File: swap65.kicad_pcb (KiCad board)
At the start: 2 copper layers, 309.6 x 100 mm, 168 parts, among them J1 USB_C_Receptacle_USB2.0, J2 OLED, J3 DB, SW1 SW_Push, SW10 A, SW11 Z, SW12 LWin, SW13 2, SW14 W, SW15 S, SW16 X, SW17 LAlt, SW18 3, SW19 E, SW2 SW_Push, SW20 D, SW21 C, SW22 4, SW23 R, SW24 F, SW25 V, SW26 5, SW27 T, SW28 G, SW29 B, SW3 Esc, SW30 Space, SW31 6, SW32 Y, SW33 H, SW34 N, SW35 7, SW36 U, SW37 J, SW38 M, SW39 8, SW4 Tab, SW40 I, SW41 K, SW42 Comma, SW43 9, SW44 O, SW45 L, SW46 Period, SW47 RAlt, SW48 0, SW49 P, SW5 Caps, SW50 Colon, SW51 Slash, SW52 Fn, SW53 Minus, SW54 [, SW55 Quote, SW56 Plus, SW57 ], SW58 RShift, SW59 Left, SW6 LShift, SW60 Pipe, SW61 BkSlsh, SW62 Enter, SW63 Up, SW64 Down, SW65 BkSpc, SW66 Tilde, SW67 Right, SW7 LCtrl, SW8 1, SW9 Q, U1 RP2040, U2 SRV05-4, U3 W25Q128JVS, U4 XC6206PxxxMR, Y1 12MHz

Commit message: routed mcu
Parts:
- moved U3 12.3 mm to (359.8, 124.2)
- moved SW1 12.2 mm to (359.1, 106.8)
- moved C1 11.7 mm to (358.4, 129.7), turned to 0 degrees
- moved R5 10.8 mm to (357.9, 113.6)
- moved R3 8.20 mm to (344.8, 146.7), turned to 0 degrees
- moved SW2 4.39 mm to (347.2, 151.7), turned to 90 degrees
- moved R1 1.33 mm to (356.4, 129.2)
- moved C13 1.31 mm to (348.4, 132.5), turned to 180 degrees
- moved C12 1.13 mm to (353.1, 128.5)
- moved C8 1.13 mm to (354.1, 128.5)
- moved R2 0.97 mm to (355.2, 129.2)
- moved C7 0.93 mm to (347.3, 137.4)
- moved R4 0.89 mm to (350.3, 140.5)
- moved C2 0.89 mm to (348.3, 143.8)
- moved C3 0.89 mm to (348.3, 139.8)
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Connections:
- U1 pad 38: SCL -> SDA
- U1 pad 39: SDA -> SCL
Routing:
- net COL1: track 0.00 -> 105.4 mm
- net COL2: track 0.00 -> 96.4 mm
- net COL13: track 0.00 -> 93.8 mm
- net COL9: track 0.00 -> 92.6 mm
- net COL10: track 0.00 -> 92.3 mm
- net COL3: track 0.00 -> 91.7 mm
- net COL5: track 0.00 -> 90.8 mm
- net COL0: track 0.00 -> 90.8 mm
- net COL12: track 0.00 -> 87.8 mm
- net COL14: track 0.00 -> 79.5 mm
- net COL7: track 0.00 -> 72.7 mm
- net COL8: track 0.00 -> 72.6 mm
- net COL6: track 0.00 -> 71.3 mm
- net +3V3: track 2.80 -> 73.5 mm
- net COL4: track 0.00 -> 70.1 mm
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- added copper zone on B.Cu, net GND

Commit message: second pass at routing complete
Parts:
- moved D10 4.77 mm to (99.2, 181.8)
- moved D5 4.77 mm to (75.4, 181.8)
- moved D15 4.76 mm to (123.0, 181.8)
- moved D45 4.76 mm to (265.9, 181.8)
- moved D50 4.76 mm to (289.7, 181.8)
- moved D49 3.22 mm to (287.3, 162.7)
- moved D14 3.21 mm to (134.9, 162.7)
- moved D19 3.21 mm to (154.0, 162.7)
- moved D27 3.21 mm to (192.1, 162.7)
- moved D36 3.21 mm to (230.2, 162.7)
- moved D4 3.21 mm to (84.9, 162.7)
- moved D40 3.21 mm to (249.2, 162.7)
- moved D44 3.21 mm to (268.3, 162.7)
- moved D56 3.21 mm to (313.5, 162.7)
- moved D61 3.21 mm to (339.7, 162.7)
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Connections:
- U1 pad 11: COL6 -> COL7
- U1 pad 12: COL5 -> COL6
- U1 pad 13: COL4 -> COL5
- U1 pad 14: COL3 -> COL4
- U1 pad 15: COL2 -> COL3
- U1 pad 16: COL1 -> COL2
- U1 pad 17: COL0 -> COL1
- U1 pad 18: unconnected-(U1-Pad18) -> COL0
- U1 pad 2: COL14 -> ROW4
- U1 pad 29: ROW4 -> unconnected-(U1-Pad29)
- U1 pad 3: COL13 -> COL14
- U1 pad 4: COL12 -> COL13
- U1 pad 5: COL11 -> COL12
- U1 pad 6: COL10 -> COL11
- U1 pad 7: COL9 -> COL10
- U1 pad 8: COL8 -> COL9
- U1 pad 9: COL7 -> COL8
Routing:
- net ROW4: track 3.87 -> 333.0 mm
- net COL0: track 90.8 -> 402.5 mm
- net ROW0: track 5.69 -> 297.6 mm
- net ROW3: track 3.53 -> 292.8 mm
- net COL1: track 105.4 -> 393.8 mm
- net ROW1: track 5.61 -> 276.3 mm
- net ROW2: track 4.58 -> 274.8 mm
- net COL2: track 96.4 -> 361.0 mm
- net COL4: track 70.1 -> 297.2 mm, vias 0 -> 1
- net COL3: track 91.7 -> 313.1 mm, vias 0 -> 1
- net COL5: track 90.8 -> 286.4 mm
- net COL6: track 71.3 -> 261.8 mm, vias 0 -> 1
- net COL7: track 72.7 -> 245.3 mm, vias 0 -> 1
- net COL8: track 72.6 -> 224.9 mm, vias 0 -> 1
- net COL9: track 92.6 -> 219.0 mm
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
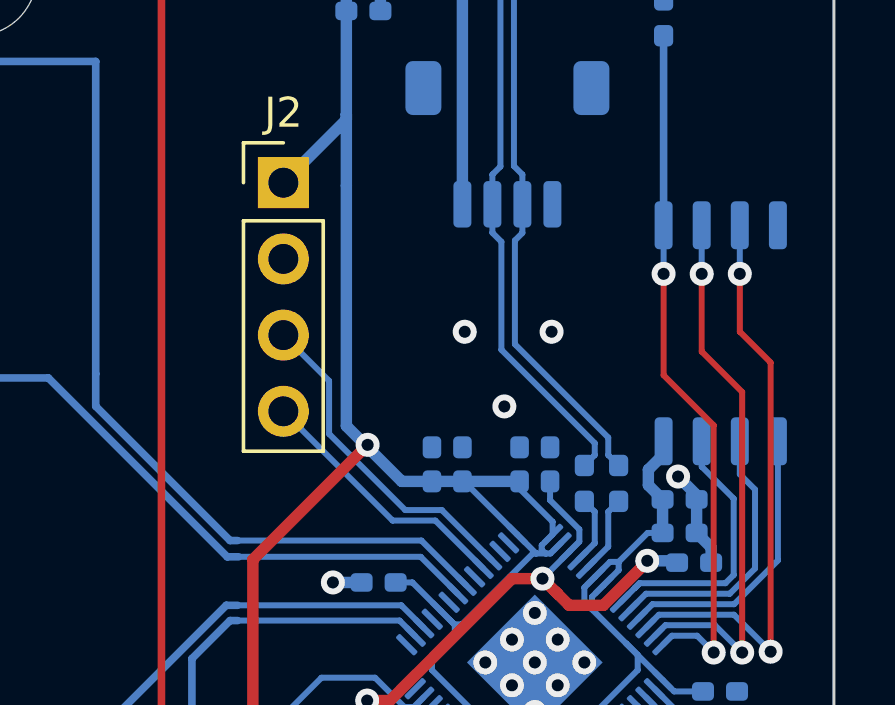
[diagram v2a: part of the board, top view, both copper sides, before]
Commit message: fixed courtyard overlap
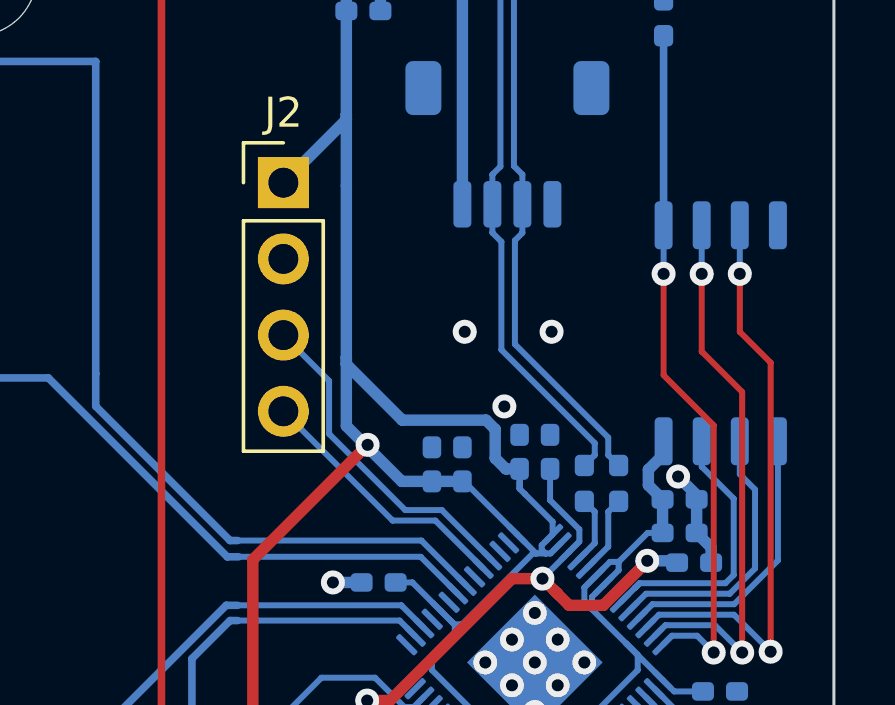
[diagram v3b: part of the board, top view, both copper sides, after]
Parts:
- moved C12 0.42 mm to (353.1, 128.1)
- moved C8 0.42 mm to (354.1, 128.1)
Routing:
- net +3V3: track 94.0 -> 100.8 mm
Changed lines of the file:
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@@
   )
   (footprint "Capacitor_SMD:C_0402_1005Metric_Pad0.74x0.62mm_HandSolder" (layer "B.Cu")
-    (at 353.06 128.524 90)
+    (at 353.06 128.1089 90)
     (descr "Capacitor SMD 0402 (1005 Metric), square (rectangular) end terminal, IPC_7351 nominal with elongated pad for handsoldering. (Body size source: IPC-SM-782 page 76, https://www.pcb-3d.com/wordpress/wp-content/uploads/ipc-sm-782a_amendment_1_and_2.pdf), generated with kicad-footprint-generator")
     (tags "capacitor handsolder")
@@
   )
   (footprint "Capacitor_SMD:C_0402_1005Metric_Pad0.74x0.62mm_HandSolder" (layer "B.Cu")
-    (at 354.076 128.524 90)
+    (at 354.076 128.1089 90)
     (descr "Capacitor SMD 0402 (1005 Metric), square (rectangular) end terminal, IPC_7351 nominal with elongated pad for handsoldering. (Body size source: IPC-SM-782 page 76, https://www.pcb-3d.com/wordpress/wp-content/uploads/ipc-sm-782a_amendment_1_and_2.pdf), generated with kicad-footprint-generator")
     (tags "capacitor handsolder")
@@
   (via (at 347.98 136.398) (size 0.8) (drill 0.4) (layers "F.Cu" "B.Cu") (net 1))
   (via (at 357.316566 131.739166) (size 0.8) (drill 0.4) (layers "F.Cu" "B.Cu") (net 1))
-  (segment (start 355.052404 131.098011) (end 355.052404 130.694204) (width 0.2) (layer "B.Cu") (net 1))
   (segment (start 347.98 136.398) (end 347.98 137.3465) (width 0.381) (layer "B.Cu") (net 1))
+  (segment (start 355.052404 131.098011) (end 355.052404 130.694204) (width 0.2) (layer "B.Cu") (net 1))
   (segment (start 357.239677 131.739166) (end 357.316566 131.739166) (width 0.2) (layer "B.Cu") (net 1))
+  (segment (start 354.725887 131.424528) (end 355.052404 131.098011) (width 0.2) (layer "B.Cu") (net 1))
+  (segment (start 354.076 129.7178) (end 354.076 128.6764) (width 0.2) (layer "B.Cu") (net 1))
   (segment (start 347.959432 137.460932) (end 350.386539 137.460932) (width 0.2) (layer "B.Cu") (net 1))
   (segment (start 347.9125 137.414) (end 347.959432 137.460932) (width 0.2) (layer "B.Cu") (net 1))
@@
   (segment (start 357.316566 131.739166) (end 358.247666 131.739166) (width 0.381) (layer "B.Cu") (net 1))
   (segment (start 354.725887 131.430113) (end 353.822 132.334) (width 0.2) (layer "B.Cu") (net 1))
-  (segment (start 354.725887 131.424528) (end 355.052404 131.098011) (width 0.2) (layer "B.Cu") (net 1))
   (segment (start 347.98 137.3465) (end 347.9125 137.414) (width 0.381) (layer "B.Cu") (net 1))
   (segment (start 355.052404 130.694204) (end 354.076 129.7178) (width 0.2) (layer "B.Cu") (net 1))
@@
   (segment (start 354.725887 131.424528) (end 354.725887 131.430113) (width 0.2) (layer "B.Cu") (net 1))
   (segment (start 356.140101 132.838742) (end 357.239677 131.739166) (width 0.2) (layer "B.Cu") (net 1))
-  (segment (start 354.076 129.7178) (end 354.076 129.0915) (width 0.2) (layer "B.Cu") (net 1))
   (via (at 354.33 135.89) (size 0.8) (drill 0.4) (layers "F.Cu" "B.Cu") (net 2))
   (via (at 355.219 135.128) (size 0.8) (drill 0.4) (layers "F.Cu" "B.Cu") (net 2))
@@
   (segment (start 347.2855 116.8567) (end 347.2855 119.2363) (width 0.381) (layer "B.Cu") (net 3))
   (segment (start 356.997 134.880045) (end 356.612977 134.496023) (width 0.2) (layer "B.Cu") (net 3))
+  (segment (start 349.1317 129.0915) (end 351.155 129.0915) (width 0.381) (layer "B.Cu") (net 3))
   (segment (start 349.2841 138.43) (end 349.983157 138.43) (width 0.2) (layer "B.Cu") (net 3))
+  (segment (start 347.2855 119.2363) (end 347.2855 124.9513) (width 0.381) (layer "B.Cu") (net 3))
   (segment (start 357.8265 129.6924) (end 357.8265 130.81) (width 0.381) (layer "B.Cu") (net 3))
   (segment (start 350.139 134.874) (end 350.139 135.382) (width 0.2) (layer "B.Cu") (net 3))
@@
   (segment (start 347.9546 127.9144) (end 349.1317 129.0915) (width 0.381) (layer "B.Cu") (net 3))
   (segment (start 353.822 138.557) (end 354.584 137.795) (width 0.2) (layer "B.Cu") (net 3))
+  (segment (start 352.2472 127.3556) (end 352.2472 128.3208) (width 0.381) (layer "B.Cu") (net 3))
   (segment (start 347.284 113.4095) (end 347.2855 113.411) (width 0.381) (layer "B.Cu") (net 3))
   (segment (start 356.997 135.382) (end 356.997 134.880045) (width 0.2) (layer "B.Cu") (net 3))
@@
   (segment (start 347.9546 127.9144) (end 347.994766 127.874234) (width 0.381) (layer "B.Cu") (net 3))
   (segment (start 357.837157 135.720202) (end 356.612977 134.496023) (width 0.2) (layer "B.Cu") (net 3))
+  (segment (start 349.1484 127.0508) (end 351.9424 127.0508) (width 0.381) (layer "B.Cu") (net 3))
   (segment (start 357.3526 128.7018) (end 357.3526 129.2185) (width 0.381) (layer "B.Cu") (net 3))
   (segment (start 356.612977 134.496023) (end 355.473 133.356045) (width 0.2) (layer "B.Cu") (net 3))
+  (segment (start 347.2855 125.1879) (end 349.1484 127.0508) (width 0.381) (layer "B.Cu") (net 3))
   (segment (start 347.2855 117.0365) (end 345.186 119.136) (width 0.381) (layer "B.Cu") (net 3))
   (segment (start 354.820787 137.795) (end 354.820787 137.558213) (width 0.2) (layer "B.Cu") (net 3))
@@
   (segment (start 357.3272 130.81) (end 357.8265 130.81) (width 0.2) (layer "B.Cu") (net 3))
   (segment (start 356.072271 131.7752) (end 356.362 131.7752) (width 0.2) (layer "B.Cu") (net 3))
+  (segment (start 353.06 129.3368) (end 353.06 128.6764) (width 0.2) (layer "B.Cu") (net 3))
   (segment (start 350.756731 133.730944) (end 350.901 133.875213) (width 0.2) (layer "B.Cu") (net 3))
   (segment (start 357.3526 129.2185) (end 357.8265 129.6924) (width 0.381) (layer "B.Cu") (net 3))
   (segment (start 350.139 135.382) (end 351.409 136.652) (width 0.2) (layer "B.Cu") (net 3))
   (segment (start 350.995899 137.417258) (end 351.380157 137.033) (width 0.2) (layer "B.Cu") (net 3))
-  (segment (start 347.2855 119.2363) (end 347.2855 127.2453) (width 0.381) (layer "B.Cu") (net 3))
   (segment (start 356.362 139.336213) (end 355.291573 138.265786) (width 0.2) (layer "B.Cu") (net 3))
   (segment (start 348.9285 132.461) (end 349.486787 132.461) (width 0.2) (layer "B.Cu") (net 3))
+  (segment (start 347.2855 124.9513) (end 347.2855 127.2453) (width 0.381) (layer "B.Cu") (net 3))
+  (segment (start 351.9424 127.0508) (end 352.2472 127.3556) (width 0.381) (layer "B.Cu") (net 3))
   (segment (start 354.820787 137.795) (end 355.291573 138.265786) (width 0.2) (layer "B.Cu") (net 3))
   (segment (start 351.79 137.033) (end 353.314 138.557) (width 0.2) (layer "B.Cu") (net 3))
-  (segment (start 349.1317 129.0915) (end 353.06 129.0915) (width 0.381) (layer "B.Cu") (net 3))
+  (segment (start 354.160202 130.437002) (end 353.2378 129.5146) (width 0.2) (layer "B.Cu") (net 3))
   (segment (start 355.574415 132.273056) (end 356.072271 131.7752) (width 0.2) (layer "B.Cu") (net 3))
+  (segment (start 352.6028 128.6764) (end 353.06 128.6764) (width 0.381) (layer "B.Cu") (net 3))
   (segment (start 347.284 110.6115) (end 347.284 113.4095) (width 0.381) (layer "B.Cu") (net 3))
   (segment (start 351.139277 133.858) (end 350.883787 133.858) (width 0.2) (layer "B.Cu") (net 3))
   (segment (start 355.473 133.356045) (end 355.473 133.35) (width 0.2) (layer "B.Cu") (net 3))
+  (segment (start 347.2855 124.9513) (end 347.2855 125.1879) (width 0.381) (layer "B.Cu") (net 3))
   (segment (start 356.362 140.0215) (end 356.362 139.336213) (width 0.2) (layer "B.Cu") (net 3))
   (segment (start 353.7966 131.3688) (end 353.7966 131.222445) (width 0.2) (layer "B.Cu") (net 3))
@@
   (segment (start 353.9236 131.4958) (end 353.7966 131.3688) (width 0.2) (layer "B.Cu") (net 3))
   (segment (start 350.901 133.875213) (end 350.901 134.112) (width 0.2) (layer "B.Cu") (net 3))
+  (segment (start 353.2378 129.5146) (end 353.06 129.3368) (width 0.2) (layer "B.Cu") (net 3))
   (segment (start 353.612755 131.4958) (end 353.949 131.4958) (width 0.2) (layer "B.Cu") (net 3))
-  (segment (start 354.160202 130.437002) (end 353.06 129.3368) (width 0.2) (layer "B.Cu") (net 3))
   (segment (start 344.17 145.542) (end 344.17 146.6983) (width 0.381) (layer "B.Cu") (net 3))
   (segment (start 354.088931 131.4958) (end 354.443045 131.141686) (width 0.2) (layer "B.Cu") (net 3))
   (segment (start 357.8606 128.1938) (end 357.3526 128.7018) (width 0.381) (layer "B.Cu") (net 3))
   (segment (start 357.8606 127.7552) (end 357.8606 128.1938) (width 0.381) (layer "B.Cu") (net 3))
+  (segment (start 352.2472 128.3208) (end 352.6028 128.6764) (width 0.381) (layer "B.Cu") (net 3))
   (segment (start 347.2855 127.2453) (end 347.9546 127.9144) (width 0.381) (layer "B.Cu") (net 3))
   (segment (start 350.756731 133.730944) (end 350.430214 133.404427) (width 0.2) (layer "B.Cu") (net 3))
